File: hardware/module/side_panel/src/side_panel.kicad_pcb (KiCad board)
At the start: 2 copper layers, 96 x 120.2 mm, 35 parts, among them J1 Top Connector, J2 Bottom Connecor, J3 Conn_01x05, J4 Conn_01x09, M1 GA12-N20 12V 100rpm, Q1 AP2302B, U1 QRE1113GR, U2 QRE1113GR, U3 QRE1113GR, U4 QRE1113GR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

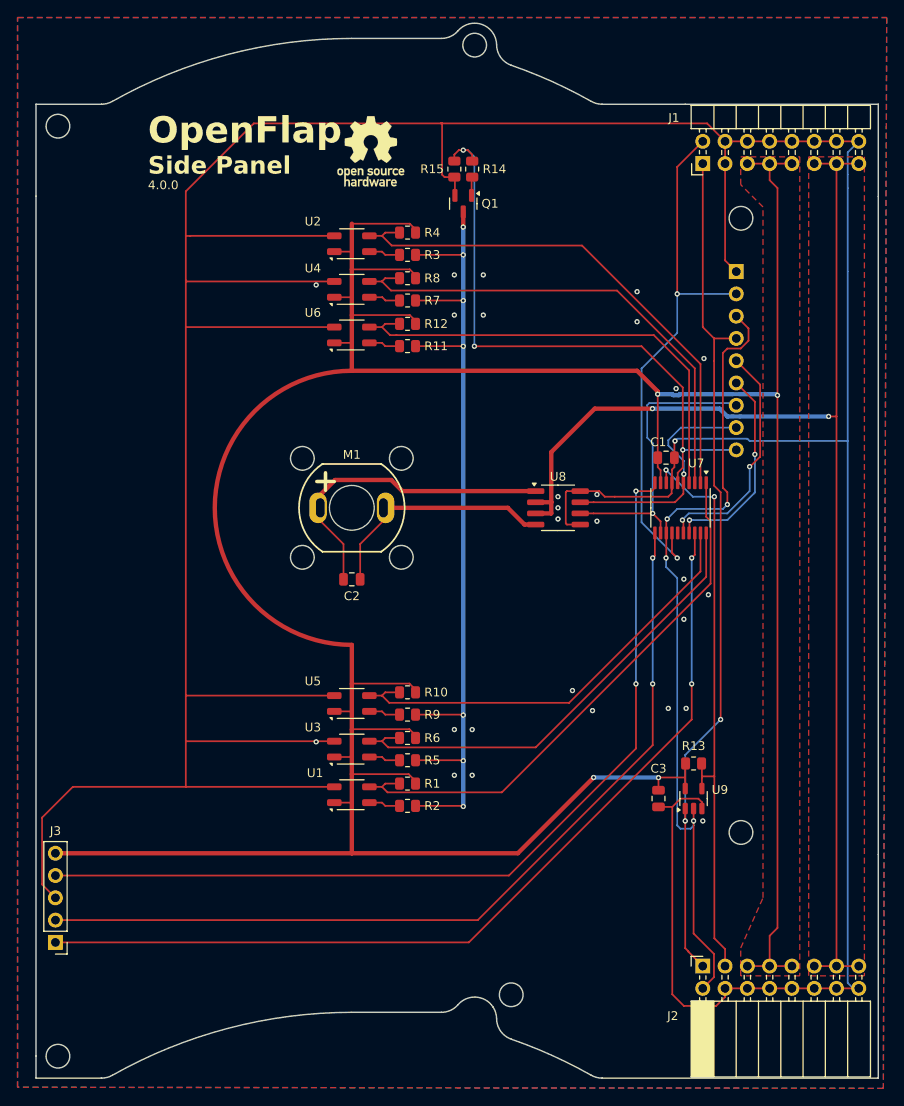
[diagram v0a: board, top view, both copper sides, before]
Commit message: Added TVS diode to UART line on side pannel
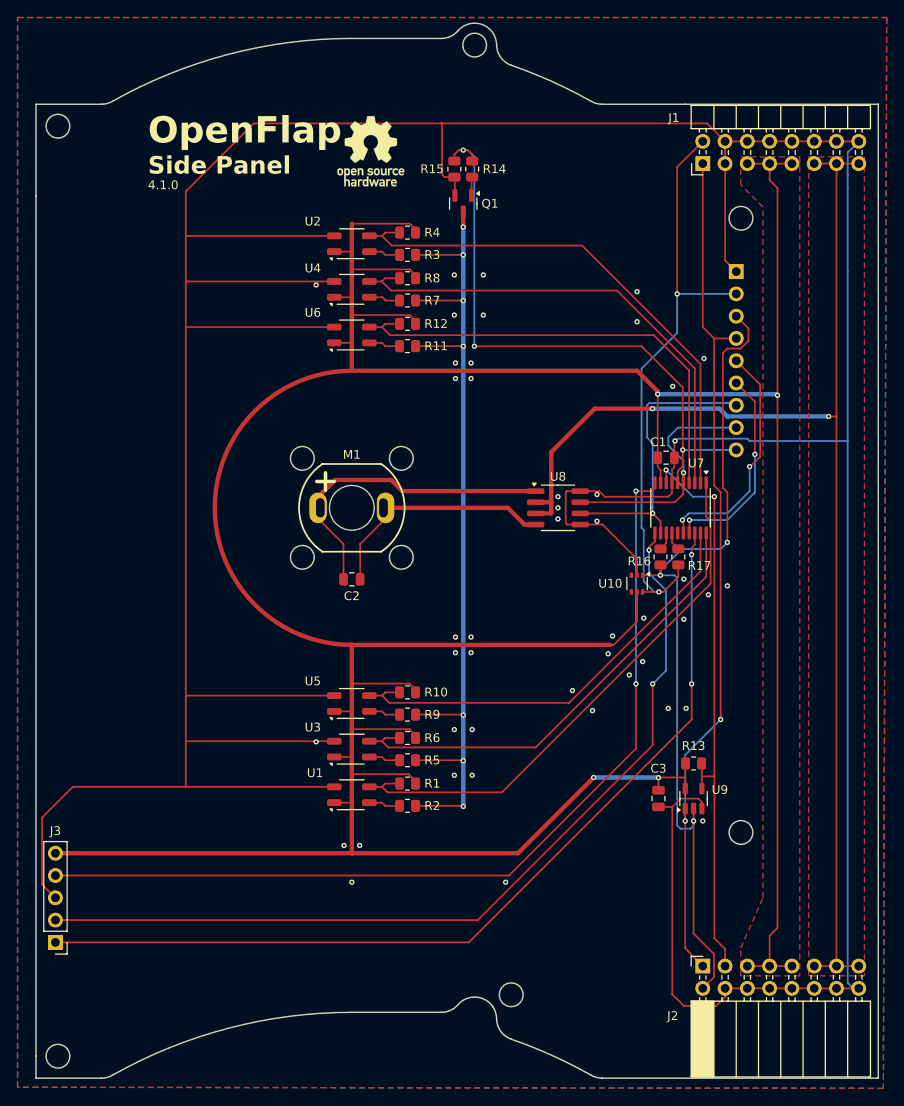
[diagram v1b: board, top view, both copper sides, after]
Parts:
- added R16: 100R, Resistor_SMD:R_0805_2012Metric, F.Cu at (132.1, 137.8)
- added R17: 100R, Resistor_SMD:R_0805_2012Metric, F.Cu at (134.2, 137.8)
- added U10: NUP4202, Package_TO_SOT_SMD:SOT-363_SC-70-6, F.Cu at (129.5, 140.8)
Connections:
- U7 pad 13: /TX Bottom -> Net-(U7-PB6)
- U7 pad 14: /RX Top -> Net-(U7-PB7)
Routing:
- net +5V: track 342.5 -> 379.4 mm
- net GND: track 495.2 -> 505.2 mm, vias 28 -> 46
- net /RX Top: track 62.0 -> 68.6 mm
- net /TX Bottom: track 92.1 -> 96.3 mm, vias 4 -> 3
- net Net-(U7-PB7): track 0.00 -> 2.11 mm
- net Net-(U7-PB6): track 0.00 -> 2.09 mm
- net /SWC: track 100.6 -> 102.2 mm

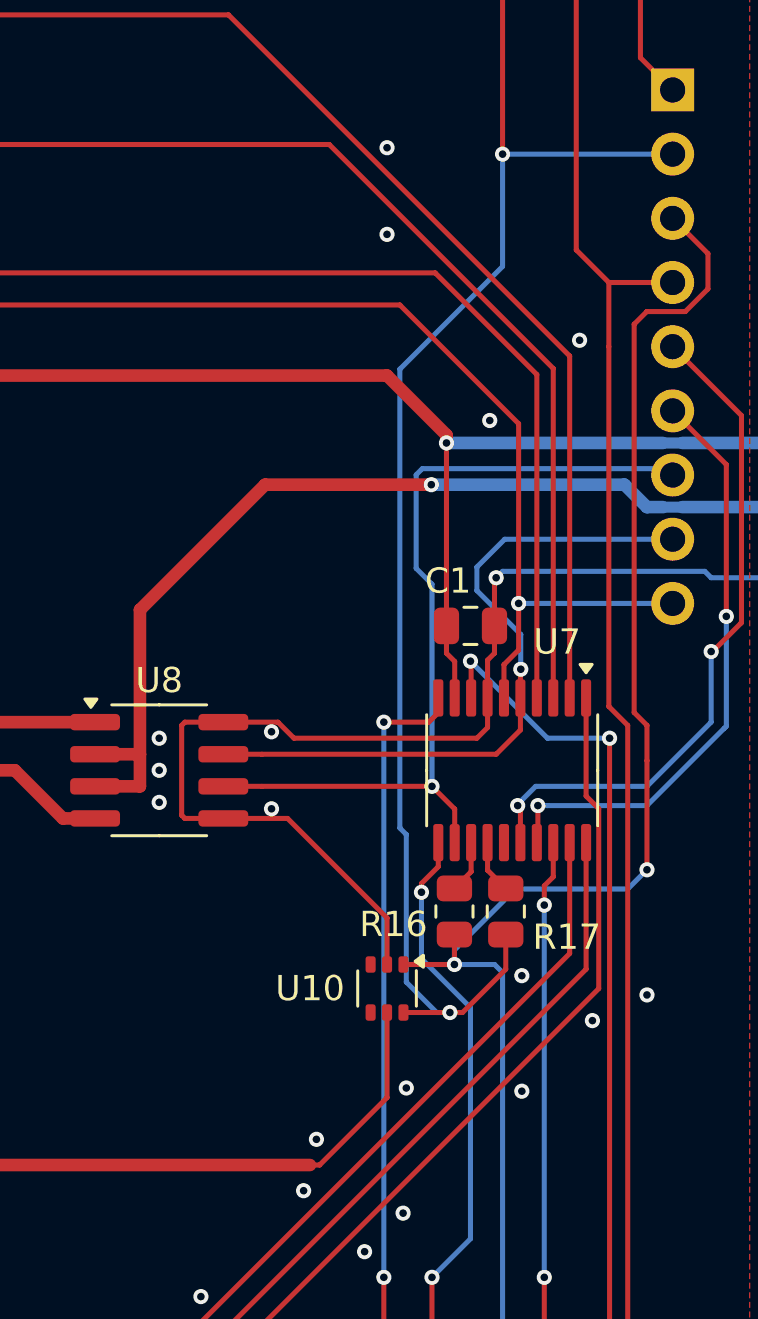
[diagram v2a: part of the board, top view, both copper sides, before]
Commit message: Added some testpads
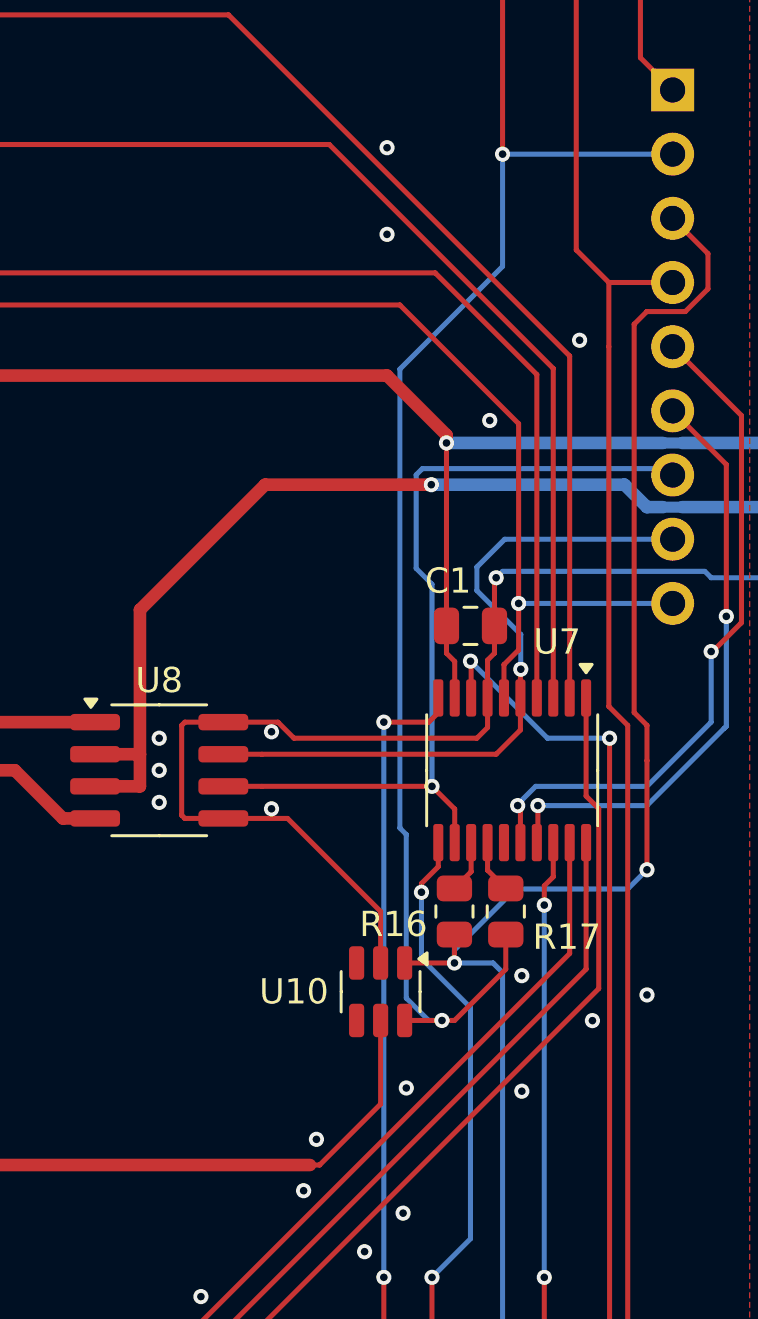
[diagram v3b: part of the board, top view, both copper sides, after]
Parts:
- U10: footprint Package_TO_SOT_SMD:SOT-363_SC-70-6 -> Package_TO_SOT_SMD:SOT-23-6
- moved U10 0.28 mm to (129.2, 140.9)

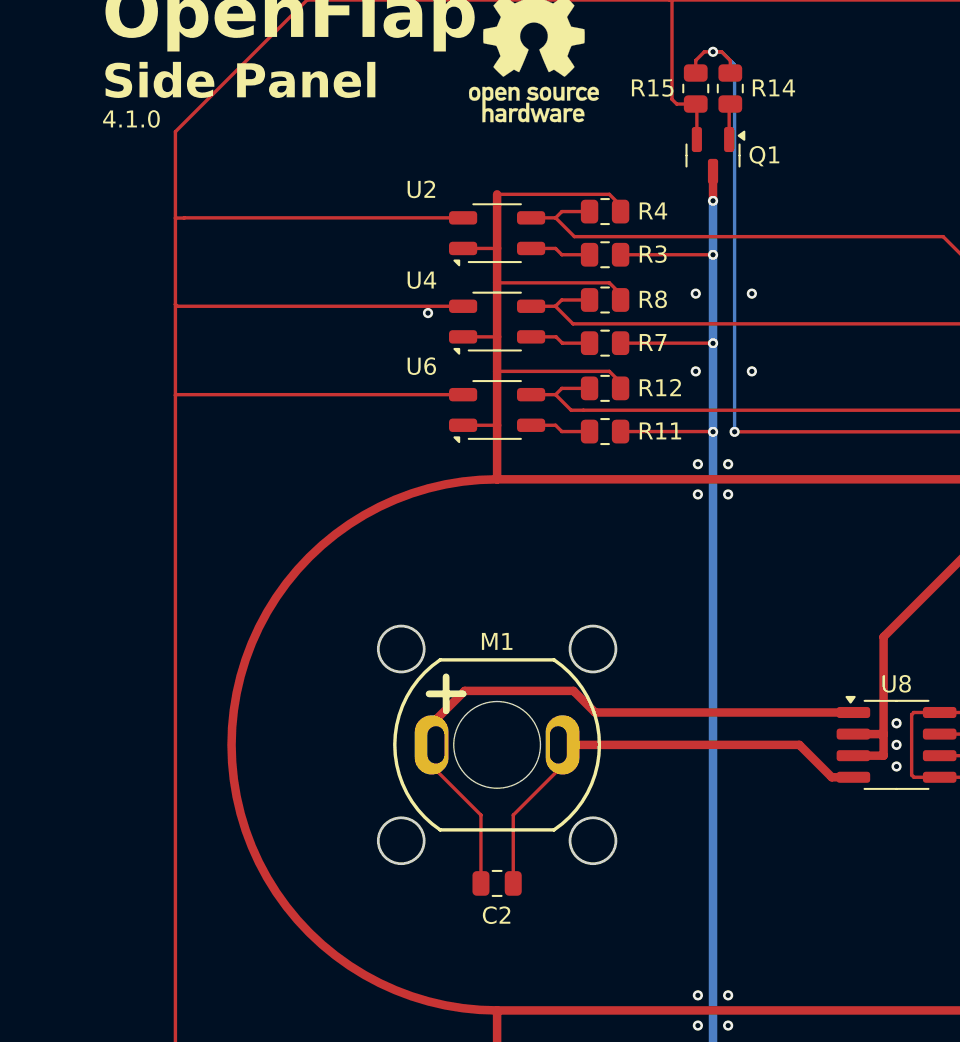
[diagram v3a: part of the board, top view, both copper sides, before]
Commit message: reverse motor polarity on side pannel
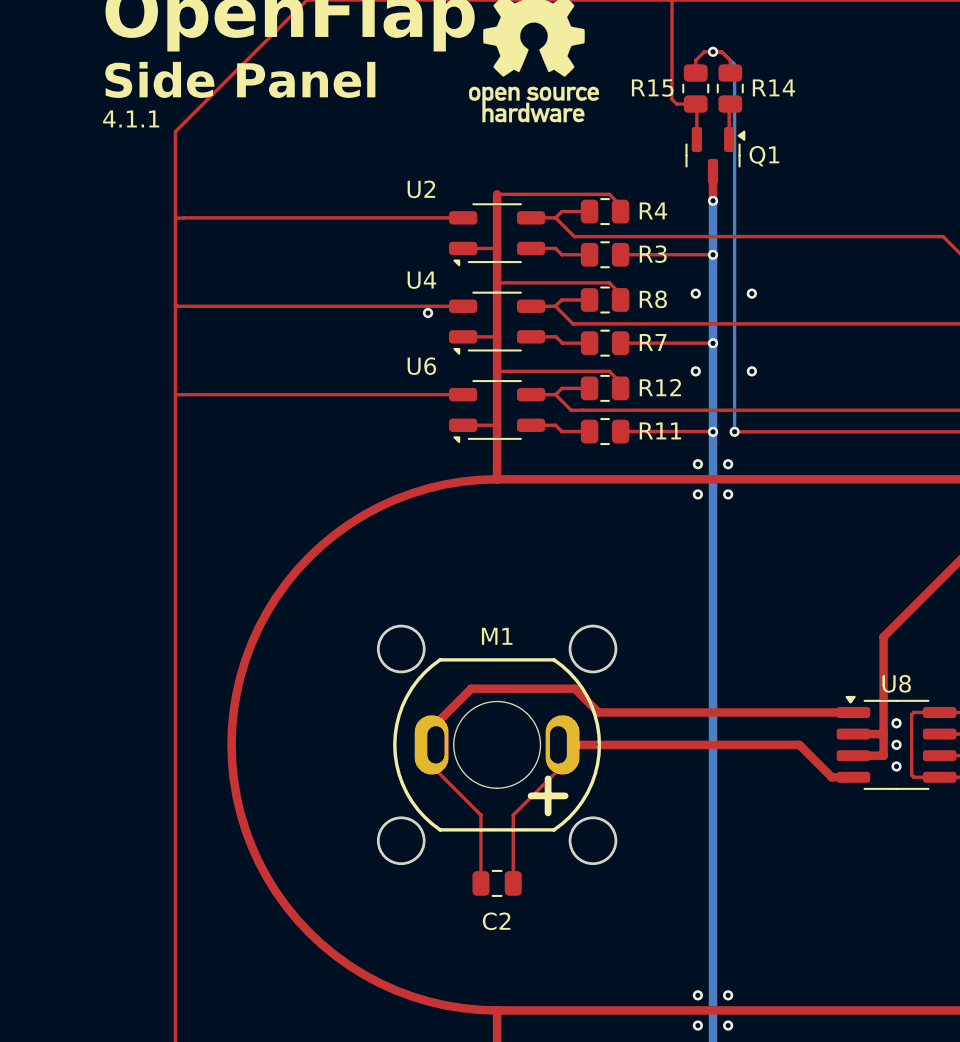
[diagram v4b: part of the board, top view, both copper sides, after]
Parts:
- turned C2 to 180 degrees
- turned M1 to 180 degrees
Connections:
- U8 pad 1: Net-(M1-+) -> Net-(M1--)
- U8 pad 4: Net-(M1--) -> Net-(M1-+)
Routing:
- net Net-(M1--): track 27.4 -> 37.9 mm
- net Net-(M1-+): track 38.0 -> 28.9 mm

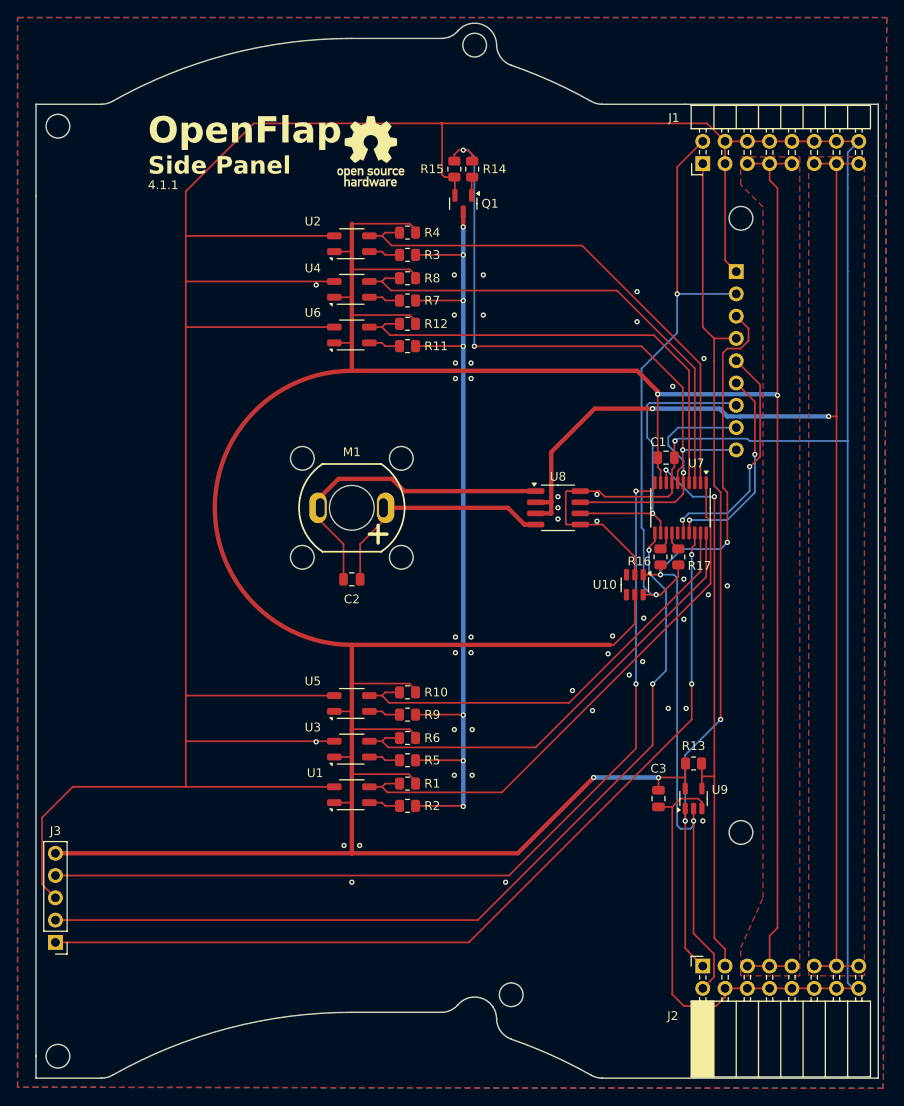
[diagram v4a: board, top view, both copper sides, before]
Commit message: remove series resistors from uart lines on modules
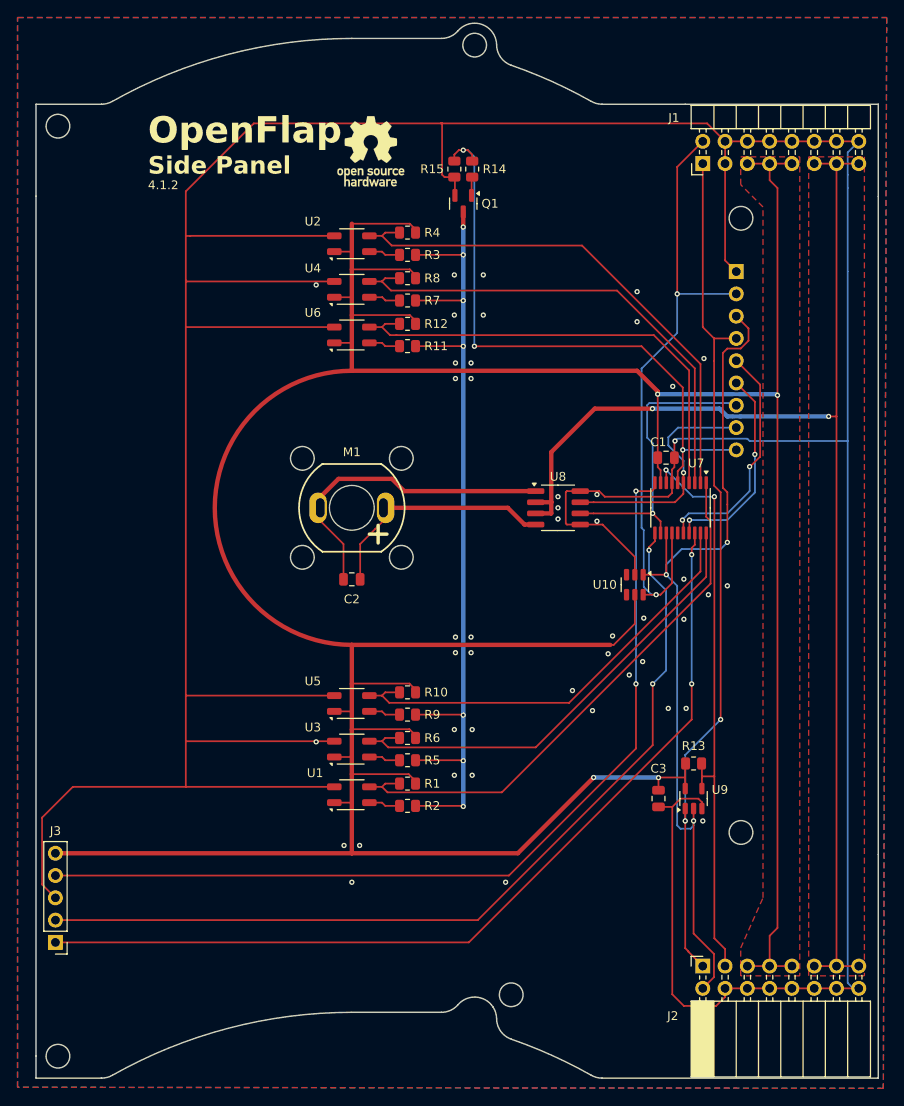
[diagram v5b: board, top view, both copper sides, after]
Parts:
- removed R16, R17: 100R, Resistor_SMD:R_0805_2012Metric
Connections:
- U7 pad 13: Net-(U7-PB6) -> /TX Bottom
- U7 pad 14: Net-(U7-PB7) -> /RX Top
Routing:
- net /RX Top: track 68.6 -> 72.0 mm
- net /TX Bottom: track 96.3 -> 99.0 mm
- net Net-(U7-PB7): track 2.11 -> 0.00 mm
- net Net-(U7-PB6): track 2.09 -> 0.00 mm

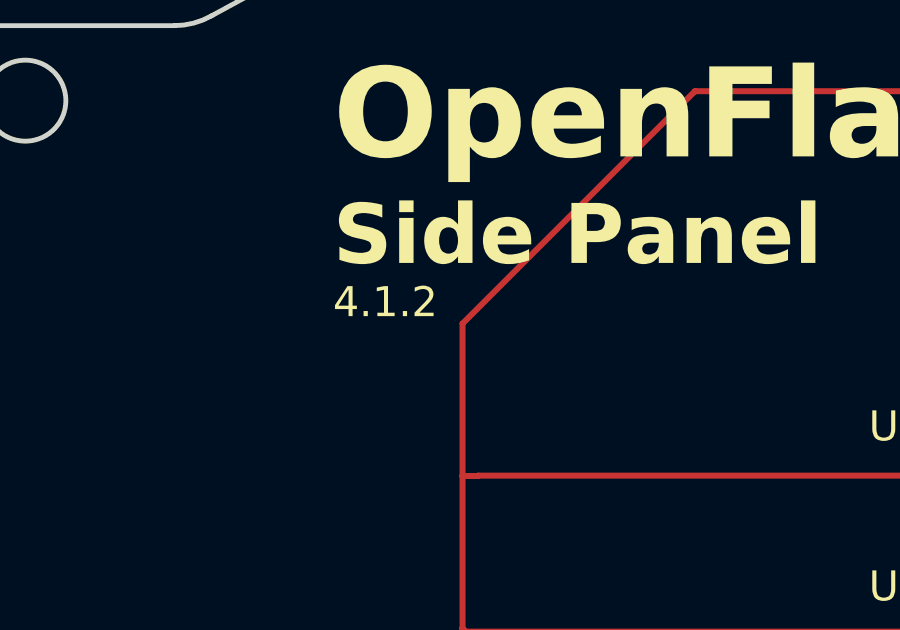
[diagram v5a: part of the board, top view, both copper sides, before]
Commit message: update side panel schematic motor RPM
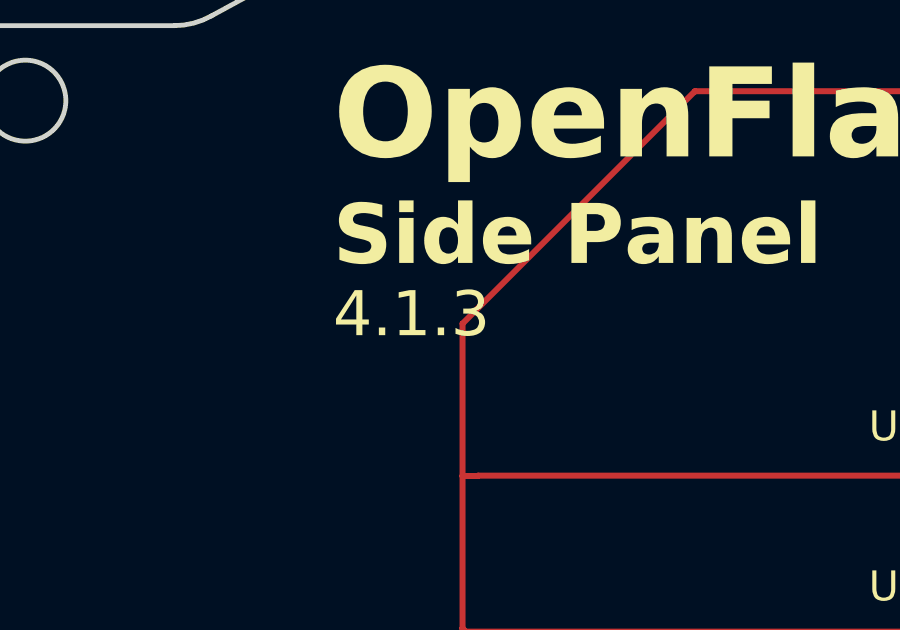
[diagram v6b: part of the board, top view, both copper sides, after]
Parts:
- M1: value GA12-N20 12V 100rpm -> GA12-N20 12V 60rpm

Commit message: wip
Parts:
- moved U1 25.0 mm to (120.1, 155.3), turned to 45 degrees
- moved R4 24.2 mm to (123.1, 114.8), turned to 0 degrees
- moved U2 23.0 mm to (118.2, 110.9), turned to 135 degrees
- moved R3 21.7 mm to (123.1, 112.2)
- moved R10 18.4 mm to (85.1, 150.1)
- moved R9 18.4 mm to (85.1, 152.6)
- moved U5 17.1 mm to (81.2, 148.0), turned to -45 degrees
- moved R12 16.2 mm to (88.2, 117.1)
- moved R11 15.1 mm to (88.2, 114.7)
- moved U6 15.1 mm to (83.0, 118.3), turned to -135 degrees
- moved R2 14.4 mm to (116.0, 159.4), turned to 0 degrees
- moved R1 14.3 mm to (116.0, 157.1), turned to 0 degrees
- moved R8 3.08 mm to (101.8, 108.7), turned to 0 degrees
- moved R7 2.96 mm to (101.8, 106.0)
- moved R6 1.27 mm to (102.0, 158.3)
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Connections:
- U7 pad 1: /IR Sens Ch 1 -> /IR Sens Ch 5
- U7 pad 19: /IR Sens Ch 5 -> /IR Sens Ch 1
- U7 pad 2: /IR Sens Ch 2 -> /IR Sens Ch 6
- U7 pad 4: /IR Sens Ch 6 -> /IR Sens Ch 2
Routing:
- net GND: track 505.0 -> 567.7 mm, vias 46 -> 59
- net /IR Sens Ch 5: track 50.8 -> 96.0 mm
- net Net-(Q1-D): track 100.5 -> 142.5 mm
- net +5V: track 378.9 -> 420.4 mm, vias 4 -> 5
- net /IR Sens Ch 6: track 53.4 -> 94.8 mm
- net /IR Sens Ch 1: track 62.9 -> 32.9 mm
- net /IR Sens Ch 2: track 59.5 -> 42.4 mm
- net /IR Sense LED: track 70.0 -> 58.5 mm
- net /IR Sens Ch 4: track 56.0 -> 66.9 mm
- net Net-(U5-K): track 3.59 -> 9.49 mm
- net Net-(U3-K): track 3.59 -> 8.06 mm
- net /IR Sens Ch 3: track 53.9 -> 58.1 mm
- net Net-(U6-K): track 3.59 -> 5.67 mm
- net Net-(U1-K): track 3.59 -> 4.74 mm
- net Net-(U2-K): track 3.59 -> 4.70 mm
